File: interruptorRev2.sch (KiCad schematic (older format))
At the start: 18 parts, among them J1 Screw_Terminal_01x02, J2 Conn_01x04, J3 Screw_Terminal_01x02, J4 Screw_Terminal_01x02, J7 Conn_01x02, Q1 2N7002, Q2 2N7002, U1 HLK-PM01, U3 ESP-07v2, U4 JRC-21(4100)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

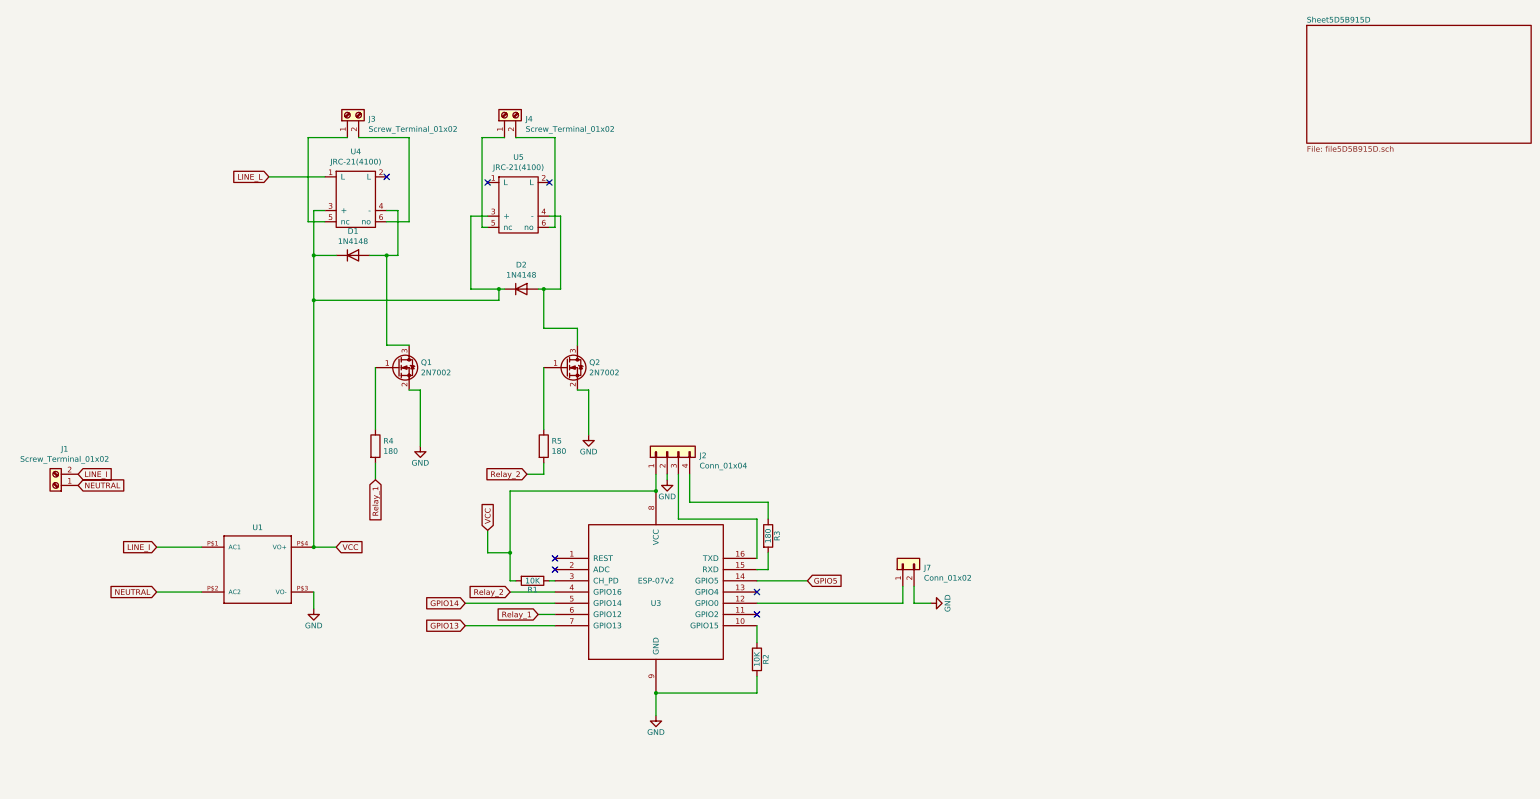
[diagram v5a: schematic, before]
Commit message: relays en esquema separado
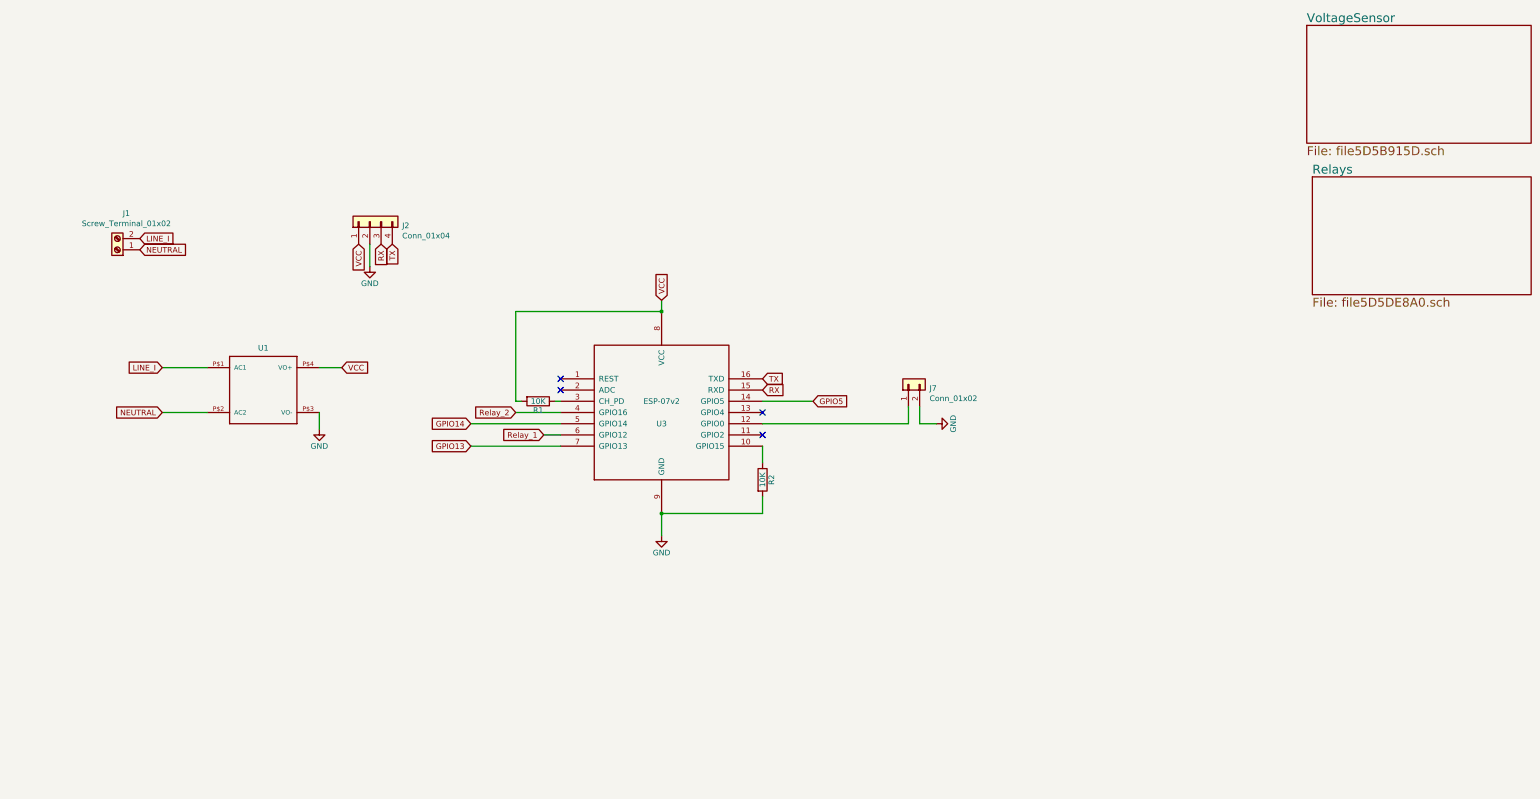
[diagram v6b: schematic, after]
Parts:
- removed D1, D2: 1N4148, espurna-h:SOD80, symbol Diode:1N4148
- removed J3, J4: Screw_Terminal_01x02, symbol Connector:Screw_Terminal_01x02
- removed Q1, Q2: 2N7002, Package_TO_SOT_SMD:SOT-23, symbol Transistor_FET:2N7002
- removed R3: 180, Resistor_SMD:R_0805_2012Metric_Pad1.15x1.40mm_HandSolder, symbol interruptorRev2-rescue:R-RESCUE-termostato-termostato-rescue-interruptor-rescue
- removed R4, R5: 180, Resistor_SMD:R_0805_2012Metric_Pad1.15x1.40mm_HandSolder, symbol Device:R
- removed U4, U5: JRC-21(4100), relays:JRC-21F, symbol interruptorRev2-rescue:JRC-21(4100)-reles
- J1: footprint (none) -> TerminalBlock:TerminalBlock_bornier-2_P5.08mm
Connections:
- net RX: now reaches U3.15 (RXD)
- net RX: now also J2.3 (Pin_3)
- net TX: now reaches U3.16 (TXD)
- net TX: now also J2.4 (Pin_4); no longer J2.3 (Pin_3)
- no-connect marks 7 -> 4
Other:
- moved on the sheet: J1, J2, J7, R1, R2, U1, U3

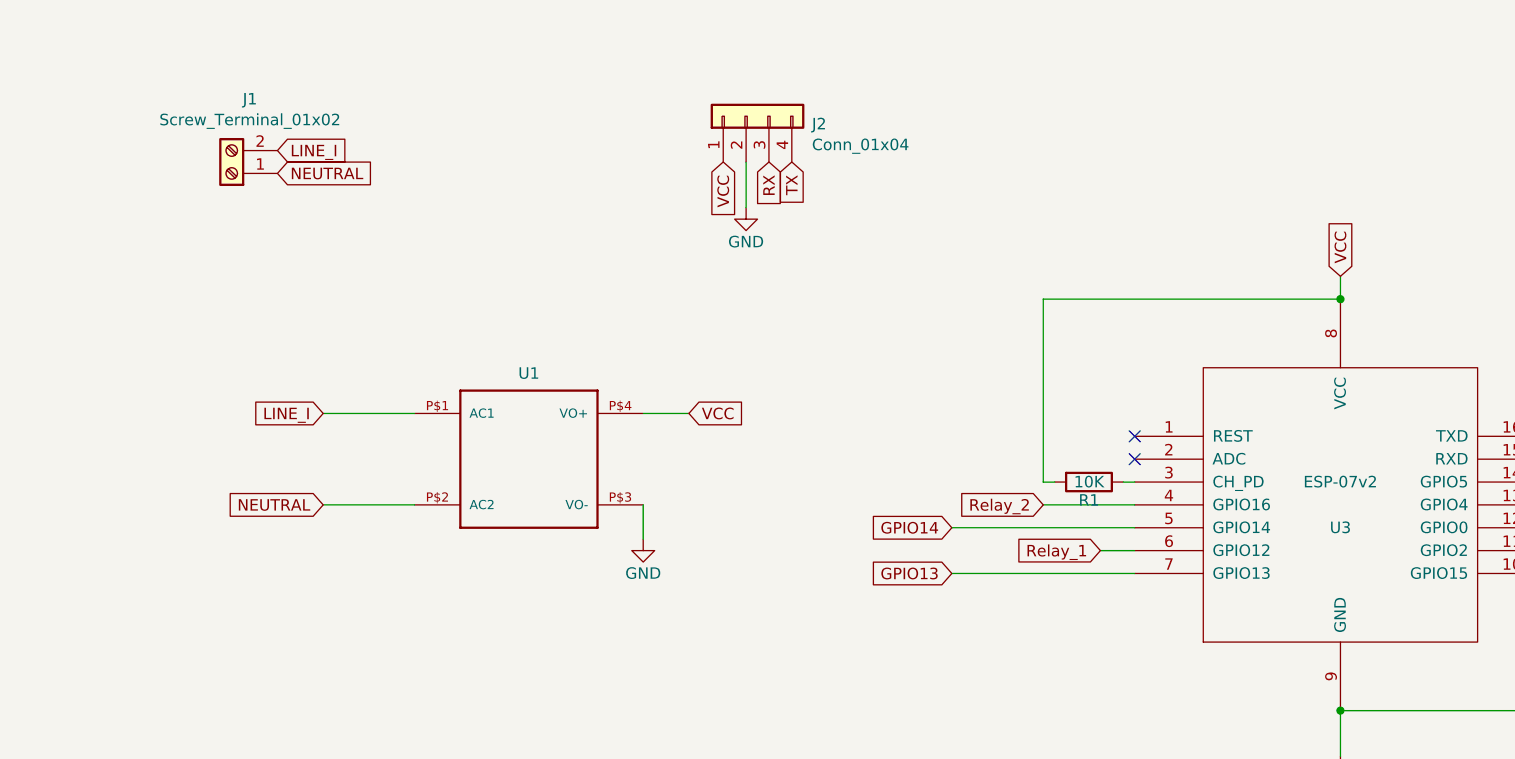
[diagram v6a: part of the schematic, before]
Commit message: regulador voltaje 3v3
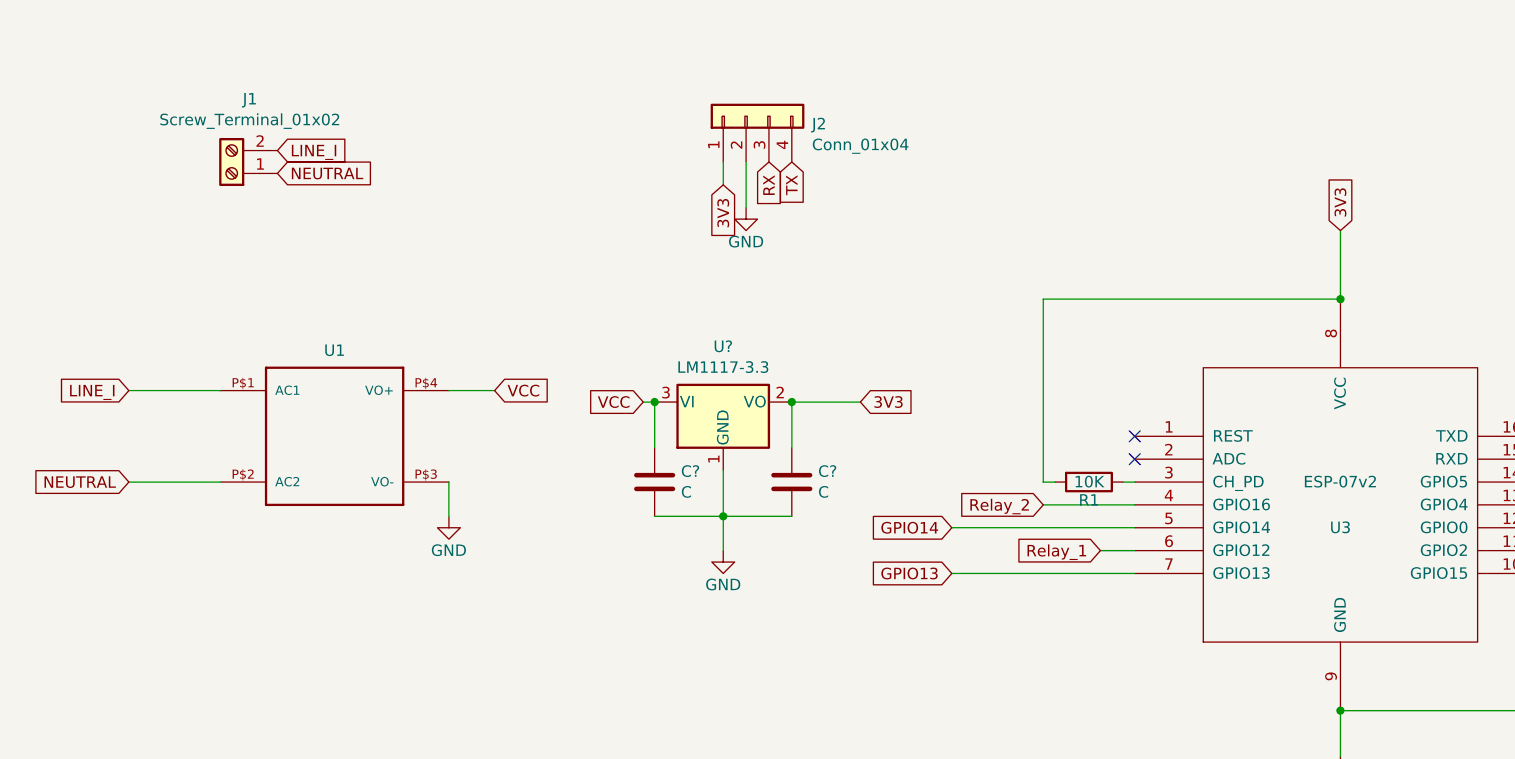
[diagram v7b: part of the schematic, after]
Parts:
- added C? (x2): C, symbol Device:C
- added U?: LM1117-3.3, symbol Regulator_Linear:LM1117-3.3
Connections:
- net GND: now also C?.2, C?.2, U?.1 (GND)
- net VCC: now also C?.1, U?.3 (VI); no longer J2.1 (Pin_1), R1.2, U3.8 (VCC)
- new net 3V3: C?.1, J2.1 (Pin_1), R1.2, U3.8 (VCC), U?.2 (VO)
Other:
- moved on the sheet: U1
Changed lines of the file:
@@
 L interruptorRev2-rescue:GND-RESCUE-termostato-termostato-rescue-interruptor-rescue #PWR?
 U 1 1 5A3E97AE
-P 3800 3700
-F 0 "#PWR?" H 3800 3450 50  0001 C CNN
-F 1 "GND" H 3800 3550 50  0000 C CNN
-F 2 "" H 3800 3700 50  0001 C CNN
-F 3 "" H 3800 3700 50  0001 C CNN
-	1    3800 3700
+P 2950 3600
+F 0 "#PWR?" H 2950 3350 50  0001 C CNN
+F 1 "GND" H 2950 3450 50  0000 C CNN
+F 2 "" H 2950 3600 50  0001 C CNN
+F 3 "" H 2950 3600 50  0001 C CNN
+	1    2950 3600
 	1    0    0    -1
 $EndComp
@@
 L interruptorRev2-rescue:HLK-PM01-HLK-PM01 U1
 U 1 1 5CD1EF95
-P 3300 3350
-F 0 "U1" H 3300 3725 50  0000 C CNN
-F 1 "HLK-PM01" H 3300 3350 50  0001 L BNN
-F 2 "HLK-PM01:HLK-PM01" H 3300 3350 50  0001 L BNN
-F 3 "Hi-link" H 3300 3350 50  0001 L BNN
-F 4 "" H 3300 3350 50  0001 L BNN "Field4"
-F 5 "hlk-pm01" H 3300 3350 50  0001 L BNN "Field5"
-F 6 "None" H 3300 3350 50  0001 L BNN "Field6"
-F 7 "Package Analog Devices" H 3300 3350 50  0001 L BNN "Field7"
-F 8 "Unavailable" H 3300 3350 50  0001 L BNN "Field8"
-	1    3300 3350
-	1    0    0    -1
-$EndComp
-Wire Wire Line
-	2400 3550 2800 3550
-Wire Wire Line
-	3800 3550 3800 3700
+P 2450 3250
+F 0 "U1" H 2450 3625 50  0000 C CNN
+F 1 "HLK-PM01" H 2450 3250 50  0001 L BNN
+F 2 "HLK-PM01:HLK-PM01" H 2450 3250 50  0001 L BNN
+F 3 "Hi-link" H 2450 3250 50  0001 L BNN
+F 4 "" H 2450 3250 50  0001 L BNN "Field4"
+F 5 "hlk-pm01" H 2450 3250 50  0001 L BNN "Field5"
+F 6 "None" H 2450 3250 50  0001 L BNN "Field6"
+F 7 "Package Analog Devices" H 2450 3250 50  0001 L BNN "Field7"
+F 8 "Unavailable" H 2450 3250 50  0001 L BNN "Field8"
+	1    2450 3250
+	1    0    0    -1
+$EndComp
+Wire Wire Line
+	1550 3450 1950 3450
+Wire Wire Line
+	2950 3450 2950 3600
 Text GLabel 5550 3550 0    50   Input ~ 0
 Relay_2
@@
 NoConn ~ 7750 3750
 Wire Wire Line
-	3800 3150 4000 3150
+	2950 3050 3150 3050
 Connection ~ 6850 4450
 $Comp
@@
 	7750 3650 9050 3650
 Wire Wire Line
-	2400 3150 2800 3150
-Text GLabel 4000 3150 2    50   Input ~ 0
-VCC
+	1550 3050 1950 3050
 $Comp
 L Connector_Generic:Conn_01x04 J2
@@
 Text GLabel 8200 3450 2    50   Input ~ 0
 GPIO5
-Text GLabel 6850 2550 1    50   Input ~ 0
-VCC
 Text GLabel 2200 2100 2    50   Input ~ 0
 NEUTRAL
-Text GLabel 2400 3550 0    50   Input ~ 0
+Text GLabel 1550 3450 0    50   Input ~ 0
 NEUTRAL
 Text GLabel 2200 2000 2    50   Input ~ 0
 LINE_I
-Text GLabel 2400 3150 0    50   Input ~ 0
+Text GLabel 1550 3050 0    50   Input ~ 0
 LINE_I
 $Comp
@@
 Wire Wire Line
 	5550 2650 6850 2650
-Wire Wire Line
-	6850 2550 6850 2650
 Connection ~ 6850 2650
 Wire Wire Line
 	5550 2650 5550 3450
-Text GLabel 4150 2050 3    50   Input ~ 0
-VCC
 $Sheet
 S 12650 1450 1950 1050
@@
 F1 "file5D5DE8A0.sch" 79
 $EndSheet
+Text GLabel 3150 3050 2    50   Input ~ 0
+VCC
+$Comp
+L Regulator_Linear:LM1117-3.3 U?
+U 1 1 5D5D81BE
+P 4150 3100
+F 0 "U?" H 4150 3342 50  0000 C CNN
+F 1 "LM1117-3.3" H 4150 3251 50  0000 C CNN
+F 2 "" H 4150 3100 50  0001 C CNN
+F 3 "http://www.ti.com/lit/ds/symlink/lm1117.pdf" H 4150 3100 50  0001 C CNN
+	1    4150 3100
+	1    0    0    -1
+$EndComp
+Text GLabel 3800 3100 0    50   Input ~ 0
+VCC
+Wire Wire Line
+	3800 3100 3850 3100
+$Comp
+L Device:C C?
+U 1 1 5D5D882E
+P 3850 3450
+F 0 "C?" H 3965 3496 50  0000 L CNN
+F 1 "C" H 3965 3405 50  0000 L CNN
+F 2 "" H 3888 3300 50  0001 C CNN
+F 3 "~" H 3850 3450 50  0001 C CNN
+	1    3850 3450
+	1    0    0    -1
+$EndComp
+Wire Wire Line
+	3850 3100 3850 3300
+Connection ~ 3850 3100
+Wire Wire Line
+	3850 3600 4150 3600
+Wire Wire Line
+	4150 3600 4150 3400
+$Comp
+L interruptorRev2-rescue:GND-RESCUE-termostato-termostato-rescue-interruptor-rescue #PWR?
+U 1 1 5D5D8EDD
+P 4150 3750
+F 0 "#PWR?" H 4150 3500 50  0001 C CNN
+F 1 "GND" H 4150 3600 50  0000 C CNN
+F 2 "" H 4150 3750 50  0001 C CNN
+F 3 "" H 4150 3750 50  0001 C CNN
+	1    4150 3750
+	1    0    0    -1
+$EndComp
+Wire Wire Line
+	4150 3600 4150 3750
+Connection ~ 4150 3600
+$Comp
+L Device:C C?
+U 1 1 5D5D928D
+P 4450 3450
+F 0 "C?" H 4565 3496 50  0000 L CNN
+F 1 "C" H 4565 3405 50  0000 L CNN
+F 2 "" H 4488 3300 50  0001 C CNN
+F 3 "~" H 4450 3450 50  0001 C CNN
+	1    4450 3450
+	1    0    0    -1
+$EndComp
+Wire Wire Line
+	4450 3100 4450 3300
+Wire Wire Line
+	4450 3600 4150 3600
+Text GLabel 4750 3100 2    50   Input ~ 0
+3V3
+Wire Wire Line
+	4450 3100 4750 3100
+Connection ~ 4450 3100
+Text GLabel 6850 2350 1    50   Input ~ 0
+3V3
+Wire Wire Line
+	6850 2350 6850 2650
+Text GLabel 4150 2150 3    50   Input ~ 0
+3V3
+Wire Wire Line
+	4150 2150 4150 2050
 $EndSCHEMATC
